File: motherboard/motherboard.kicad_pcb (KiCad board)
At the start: 4 copper layers, 177 x 88 mm, 306 parts, among them CN1 PJ-332A-6A (3.5mm Jack), IC1 PI6C557-05BLE, J1 USB_C_Receptacle, J10 DEBUG UART, J11 SYSTEM, J12 5V FAN, J13 Bus_M.2_Socket_E, J14 Micro_SD_Card_Det1, J15 Bus_M.2_Socket_M, J16 USB, J17 USB, J18 USB, J19 USB, J2 20455-040E-76 OLED IPEX, J20 CM3588 Hirose Connector, J21 5V IN, J22 BATTERY IN, J23 L829-1J1T-JM, J3 RIGHT SPEAKERS, J4 LEFT SPEAKERS, J5 Outer USB-C, J6 OLED EL POWER, J7 RTC BATTERY, J8 HDMI_A, J9 Inner USB-C, Q1 2SK3018W, Q10 2SK3018W, Q11 AO3415A, Q12 2SK3018W, Q2 2SK3018W, Q3 L2N7002WT1G, Q4 2SK3018W, Q5 2SK3018W, Q6 WNM6002-3/TR, Q7 WNM6002-3/TR, Q8 WNM6002-3/TR, Q9 WNM6002-3/TR, SW1 PWR, SW2 RESET, SW3 MASK, SW4 RECOVERY, U1 TPD4EUSB30, U10 TPD4EUSB30, U11 TPD4EUSB30, U12 TPD4EUSB30, U13 TPD4EUSB30, U14 AP2331, U16 TPD4EUSB30, U17 TPD4EUSB30, U18 TPD4EUSB30, U19 TPD4EUSB30, U2 TPD4EUSB30, U20 TPS54331DR, U21 AP2127K-3.3, U22 CH334F, U23 TPA2028D1YZFT, U24 SOT23 Hall Effect Sensor, U25 TPA2028D1YZFT, U26 AMS1117-1.8, U27 TPS54331DR, U28 SPI Flash, U3 TPD4EUSB30, U4 FUSB302BMPX, U5 SY6280AAC, U6 SY6280AAC, U7 FUSB302BMPX, U8 TPD4EUSB30, U9 TPD4EUSB30, Y1 25MHz, Y2 12MHz

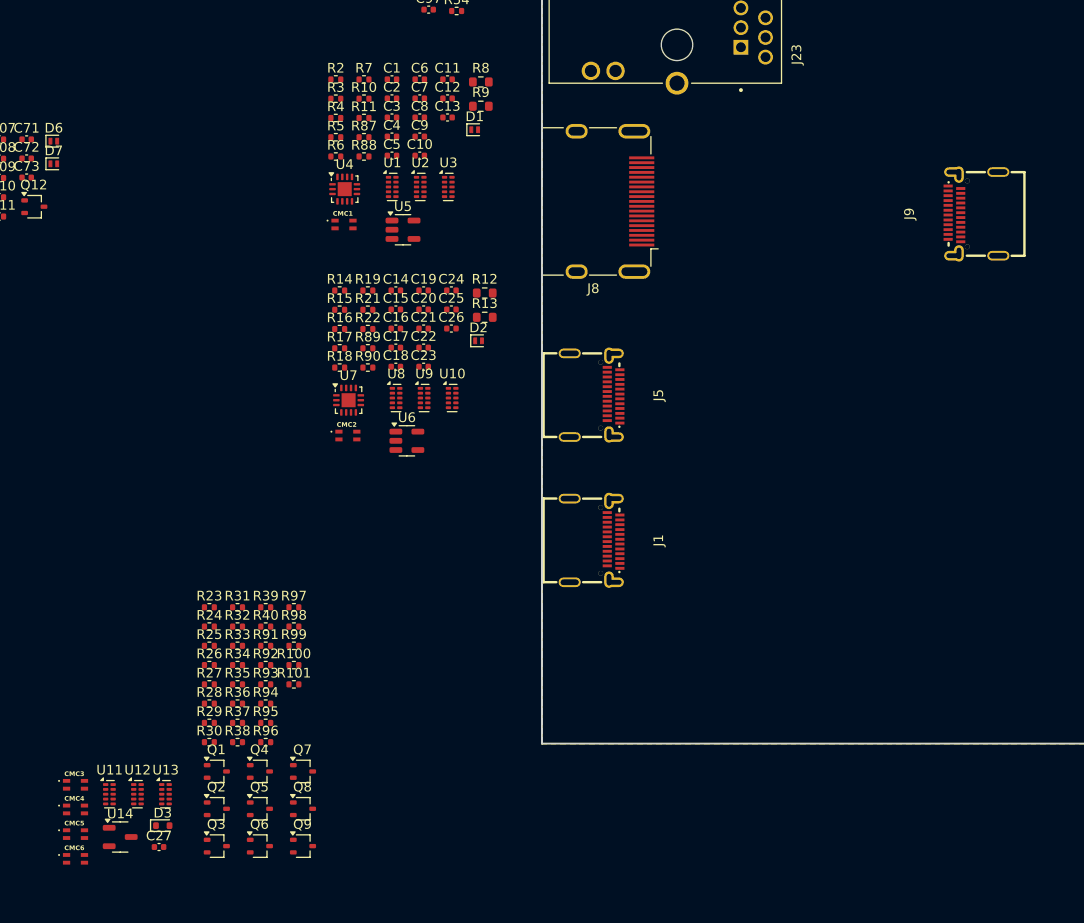
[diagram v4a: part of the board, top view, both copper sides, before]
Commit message: component placement of I/O
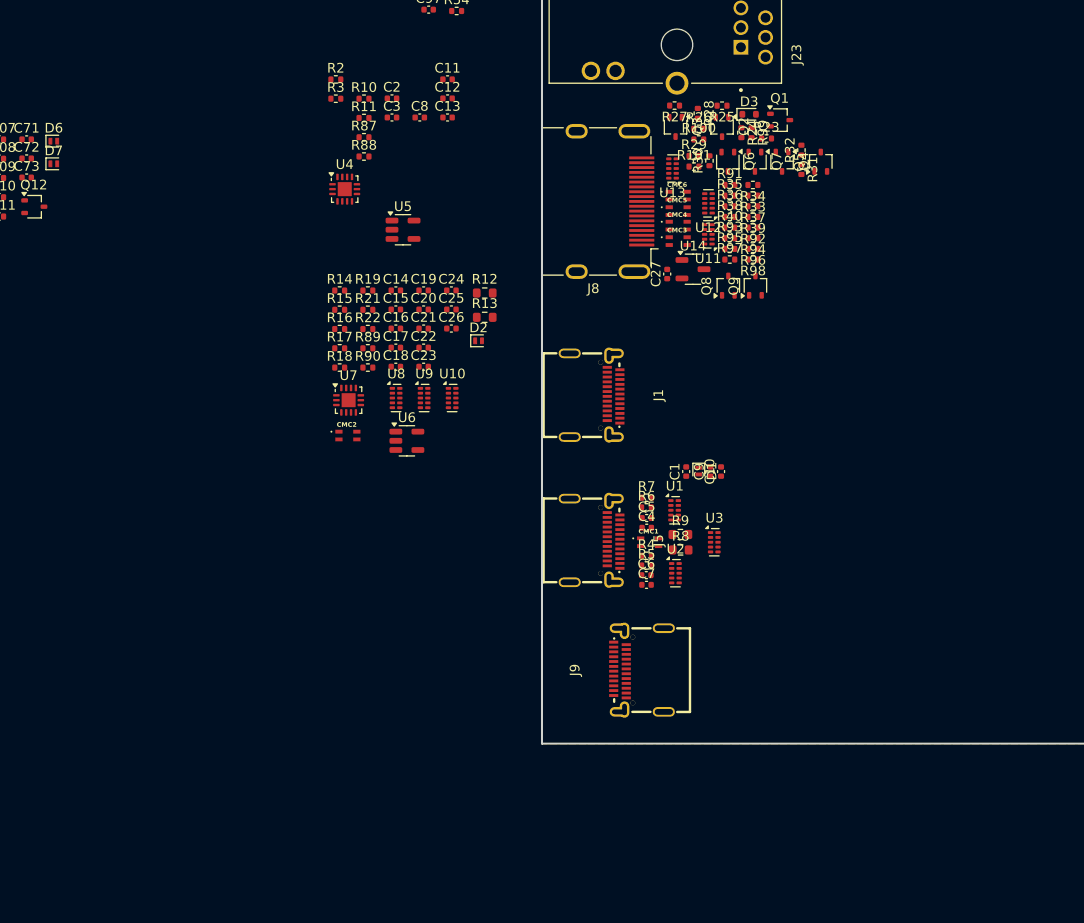
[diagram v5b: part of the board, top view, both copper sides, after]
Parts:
- moved D3 95.2 mm to (52.4, 60.0)
- moved CMC6 92.6 mm to (45.1, 68.4)
- moved CMC5 89.5 mm to (45.1, 70.0)
- moved Q1 88.9 mm to (55.6, 60.6)
- moved Q5 88.4 mm to (59.8, 64.9), turned to 90 degrees
- moved Q3 88.1 mm to (44.8, 61.3), turned to -90 degrees
- moved Q2 87.6 mm to (49.6, 61.3), turned to -90 degrees
- moved CMC4 86.7 mm to (45.1, 71.5)
- moved Q6 85.6 mm to (50.2, 64.9), turned to -90 degrees
- moved U12 84.9 mm to (48.2, 69.2), turned to 180 degrees
- moved U11 84.7 mm to (48.2, 72.4), turned to 180 degrees
- moved CMC3 83.8 mm to (45.1, 73.1)
- moved U14 83.3 mm to (46.6, 76.0)
- moved U13 83.2 mm to (44.5, 65.6), turned to 180 degrees
- moved Q4 82.9 mm to (55.8, 64.9), turned to -90 degrees
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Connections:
- CMC1 pad 1: /USBC0/IN_D- -> /USBC0/IN_D+
- CMC1 pad 2: /USBC0/IN_D+ -> /USBC0/IN_D-
- CMC1 pad 3: unconnected-(R9-Pad1) -> unconnected-(R8-Pad1)
- CMC1 pad 4: unconnected-(R8-Pad1) -> unconnected-(R9-Pad1)
- CMC10 pad 1: /P25G_MDIP3 -> /P25G_MDIN3
- CMC10 pad 2: /P25G_MDIN3 -> /P25G_MDIP3
- CMC10 pad 3: /Ethernet/N3 -> /Ethernet/P3
- CMC10 pad 4: /Ethernet/P3 -> /Ethernet/N3
- CMC3 pad 3: /HDMI_TX/HDMI0_TX2N_PORT -> /HDMI_TX/HDMI0_TX2P_PORT
- CMC3 pad 4: /HDMI_TX/HDMI0_TX2P_PORT -> /HDMI_TX/HDMI0_TX2N_PORT
- CMC4 pad 3: /HDMI_TX/HDMI0_TX1N_PORT -> /HDMI_TX/HDMI0_TX1P_PORT
- CMC4 pad 4: /HDMI_TX/HDMI0_TX1P_PORT -> /HDMI_TX/HDMI0_TX1N_PORT
- CMC5 pad 3: /HDMI_TX/HDMI0_TX0N_PORT -> /HDMI_TX/HDMI0_TX0P_PORT
- CMC5 pad 4: /HDMI_TX/HDMI0_TX0P_PORT -> /HDMI_TX/HDMI0_TX0N_PORT
- CMC6 pad 3: /HDMI_TX/HDMI0_TX3N_PORT -> /HDMI_TX/HDMI0_TX3P_PORT
- CMC6 pad 4: /HDMI_TX/HDMI0_TX3P_PORT -> /HDMI_TX/HDMI0_TX3N_PORT
- CMC7 pad 1: /P25G_MDIP2 -> /P25G_MDIN2
- CMC7 pad 2: /P25G_MDIN2 -> /P25G_MDIP2
- CMC7 pad 3: /Ethernet/N0 -> /Ethernet/P0
- CMC7 pad 4: /Ethernet/P0 -> /Ethernet/N0
- CMC8 pad 1: /P25G_MDIP1 -> /P25G_MDIN1
- CMC8 pad 2: /P25G_MDIN1 -> /P25G_MDIP1
- CMC8 pad 3: /Ethernet/N1 -> /Ethernet/P1
- CMC8 pad 4: /Ethernet/P1 -> /Ethernet/N1
- CMC9 pad 1: /P25G_MDIP0 -> /P25G_MDIN0
- CMC9 pad 2: /P25G_MDIN0 -> /P25G_MDIP0
- CMC9 pad 3: /Ethernet/N2 -> /Ethernet/P2
- CMC9 pad 4: /Ethernet/P2 -> /Ethernet/N2
- J1 pad A6: Net-(CMC2-Pad2) -> Net-(CMC2-Pad1)
- J1 pad A7: Net-(CMC2-Pad1) -> Net-(CMC2-Pad2)
- J1 pad B6: Net-(CMC2-Pad2) -> Net-(CMC2-Pad1)
- J1 pad B7: Net-(CMC2-Pad1) -> Net-(CMC2-Pad2)
- J8 pad 1: unconnected-(CMC3-Pad1) -> unconnected-(CMC3-Pad2)
- J8 pad 10: unconnected-(CMC6-Pad1) -> unconnected-(CMC6-Pad2)
- J8 pad 12: unconnected-(CMC6-Pad2) -> unconnected-(CMC6-Pad1)
- J8 pad 3: unconnected-(CMC3-Pad2) -> unconnected-(CMC3-Pad1)
- J8 pad 4: unconnected-(CMC4-Pad1) -> unconnected-(CMC4-Pad2)
- J8 pad 6: unconnected-(CMC4-Pad2) -> unconnected-(CMC4-Pad1)
- J8 pad 7: unconnected-(CMC5-Pad1) -> unconnected-(CMC5-Pad2)
- J8 pad 9: unconnected-(CMC5-Pad2) -> unconnected-(CMC5-Pad1)
- R12 pad 1: Net-(CMC2-Pad4) -> Net-(CMC2-Pad3)
- R13 pad 1: Net-(CMC2-Pad3) -> Net-(CMC2-Pad4)
- U1 pad 10: unconnected-(U1-NC-Pad10) -> /USBC0/RX1+
- U1 pad 6: unconnected-(U1-NC-Pad6) -> /USBC0/TX1-
- U1 pad 7: unconnected-(U1-NC-Pad7) -> /USBC0/TX1+
- U1 pad 9: unconnected-(U1-NC-Pad9) -> /USBC0/RX1-
- U11 pad 10: unconnected-(U11-NC-Pad10) -> /HDMI_TX/HDMI0_TX2P_PORT
- U11 pad 6: unconnected-(U11-NC-Pad6) -> /HDMI_TX/HDMI0_TX1N_PORT
- U11 pad 7: unconnected-(U11-NC-Pad7) -> /HDMI_TX/HDMI0_TX1P_PORT
- U11 pad 9: unconnected-(U11-NC-Pad9) -> /HDMI_TX/HDMI0_TX2N_PORT
- U12 pad 10: unconnected-(U12-NC-Pad10) -> /HDMI_TX/HDMI0_TX0P_PORT
- U12 pad 6: unconnected-(U12-NC-Pad6) -> /HDMI_TX/HDMI0_TX3N_PORT
- U12 pad 7: unconnected-(U12-NC-Pad7) -> /HDMI_TX/HDMI0_TX3P_PORT
- U12 pad 9: unconnected-(U12-NC-Pad9) -> /HDMI_TX/HDMI0_TX0N_PORT
- U13 pad 10: unconnected-(U13-NC-Pad10) -> /HDMI_TX/CEC
- U13 pad 2: /HDMI_TX/HDMI0_5V -> /HDMI_TX/SBDP
- U13 pad 4: /HDMI_TX/SBDP -> /HDMI_TX/HDMI0_5V
- U13 pad 6: unconnected-(U13-NC-Pad6) -> /HDMI_TX/SBDN
- U13 pad 7: unconnected-(U13-NC-Pad7) -> /HDMI_TX/HDMI0_5V
- U13 pad 9: unconnected-(U13-NC-Pad9) -> /HDMI_TX/SBDP
- U2 pad 10: unconnected-(U2-NC-Pad10) -> /USBC0/RX2-
- U2 pad 4: /USBC0/TX2+ -> /USBC0/TX2-
- U2 pad 5: /USBC0/TX2- -> /USBC0/TX2+
- U2 pad 6: unconnected-(U2-NC-Pad6) -> /USBC0/TX2+
- U2 pad 7: unconnected-(U2-NC-Pad7) -> /USBC0/TX2-
- U2 pad 9: unconnected-(U2-NC-Pad9) -> /USBC0/RX2+
- U3 pad 10: unconnected-(U3-NC-Pad10) -> /USBC0/D+
- U3 pad 4: /USBC0/SBUS1 -> /USBC0/SBUS2
- U3 pad 5: /USBC0/SBUS2 -> /USBC0/SBUS1
- U3 pad 6: unconnected-(U3-NC-Pad6) -> /USBC0/SBUS1
- U3 pad 7: unconnected-(U3-NC-Pad7) -> /USBC0/SBUS2
- U3 pad 9: unconnected-(U3-NC-Pad9) -> /USBC0/D-

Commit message: placement roughly halfway done
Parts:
- removed C17, C18, C21, C22, C33, C34, C4, C5, C6, C7: 100nF, Capacitor_SMD:C_0402_1005Metric
- removed C37, C38, C39, C40, C41, C42, C43, C44: 220nF, Capacitor_SMD:C_0402_1005Metric
- removed D1, D2: LESD8D5.0CB1T5G, Diode_SMD:D_SOD-882
- removed R12, R13, R8, R9: 2.2R, Resistor_SMD:R_0603_1608Metric
- removed R14, R15, R16, R17, R4, R5, R6, R7: 0R, Resistor_SMD:R_0402_1005Metric
- added U15: TVS2200DRV, Package_SON:WSON-6-1EP_2x2mm_P0.65mm_EP1x1.6mm, F.Cu at (34.1, 39.6)
- added U29: TVS2200DRV, Package_SON:WSON-6-1EP_2x2mm_P0.65mm_EP1x1.6mm, F.Cu at (76.5, 64.6)
- C1, C14: value 100nF -> 100nF (+25V)
- C10, C15, C16, C9: value 10uF -> 10uF (C913517); footprint Capacitor_SMD:C_0402_1005Metric -> Capacitor_SMD:C_0603_1608Metric
- C94, C95, C96, C97: footprint Capacitor_SMD:C_0402_1005Metric -> Capacitor_SMD:C_0805_2012Metric
- U1, U10, U11, U12, U13, U16, U17, U18, U19, U2, U3, U8, U9: value TPD4EUSB30 -> TPD4E02B04
- moved CN1 203.3 mm to (141.5, 156.5), turned to 180 degrees
- moved R102 195.2 mm to (145.7, 151.7), turned to 180 degrees
- moved R104 190.5 mm to (137.0, 161.8), turned to 180 degrees
- moved R107 186.8 mm to (134.5, 159.7)
- moved D7 186.8 mm to (140.8, 161.1), turned to -90 degrees
- moved R103 186.6 mm to (137.3, 151.2), turned to 180 degrees
- moved R106 185.4 mm to (133.6, 161.4), turned to -90 degrees
- moved C72 184.7 mm to (135.1, 161.4), turned to 90 degrees
- moved R109 184.3 mm to (135.2, 157.6), turned to -90 degrees
- moved R108 182.7 mm to (134.7, 153.2)
- moved R110 182.4 mm to (135.2, 155.6), turned to -90 degrees
- moved D6 182.0 mm to (139.5, 151.5), turned to 90 degrees
- moved R105 181.9 mm to (133.8, 151.6), turned to 90 degrees
- moved R111 181.4 mm to (133.7, 158.2)
- moved C71 180.9 mm to (135.3, 151.6), turned to -90 degrees
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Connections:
- net Net-(U25-EN) renamed /Audio/SPK_EN_L
- CMC1 pad 3: unconnected-(R8-Pad1) -> /USBC0/D-
- CMC1 pad 4: unconnected-(R9-Pad1) -> /USBC0/D+
- CMC2 pad 3: Net-(CMC2-Pad3) -> /USBC1/D-
- CMC2 pad 4: Net-(CMC2-Pad4) -> /USBC1/D+
- J1 pad A10: Net-(J1-RX2-) -> /USBC1/RX2-
- J1 pad A11: Net-(J1-RX2+) -> /USBC1/RX2+
- J1 pad A2: Net-(J1-TX1+) -> /USBC1/TX1+
- J1 pad A3: Net-(J1-TX1-) -> /USBC1/TX1-
- J1 pad B10: Net-(J1-RX1-) -> /USBC1/RX1-
- J1 pad B11: Net-(J1-RX1+) -> /USBC1/RX1+
- J1 pad B2: Net-(J1-TX2+) -> /USBC1/TX2+
- J1 pad B3: Net-(J1-TX2-) -> /USBC1/TX2-
- J13 pad 35: unconnected-(C33-Pad2) -> /PCIE20_1_TXP
- J13 pad 37: unconnected-(C34-Pad2) -> /PCIE20_1_TXN
- J15 pad 11: Net-(J15-PETn3) -> /PCIE30_PORT1_TX3N
- J15 pad 13: Net-(J15-PETp3) -> /PCIE30_PORT1_TX3P
- J15 pad 23: Net-(J15-PETn2) -> /PCIE30_PORT1_TX2N
- J15 pad 25: Net-(J15-PETp2) -> /PCIE30_PORT1_TX2P
- J15 pad 35: Net-(J15-PETn1) -> /PCIE30_PORT0_TX1N
- J15 pad 37: Net-(J15-PETp1) -> /PCIE30_PORT0_TX1P
- J15 pad 47: Net-(J15-PETn0/SATA-A-) -> /PCIE30_PORT0_TX0N
- J15 pad 49: Net-(J15-PETp0/SATA-A+) -> /PCIE30_PORT0_TX0P
- J5 pad A10: /USBC0/IN_RX2- -> /USBC0/RX2-
- J5 pad A11: /USBC0/IN_RX2+ -> /USBC0/RX2+
- J5 pad A2: /USBC0/IN_TX1+ -> /USBC0/TX1+
- J5 pad A3: /USBC0/IN_TX1- -> /USBC0/TX1-
- J5 pad B10: /USBC0/IN_RX1- -> /USBC0/RX1-
- J5 pad B11: /USBC0/IN_RX1+ -> /USBC0/RX1+
- J5 pad B2: /USBC0/IN_TX2+ -> /USBC0/TX2+
- J5 pad B3: /USBC0/IN_TX2- -> /USBC0/TX2-
- J9 pad A10: /USBC0/IN_RX2- -> /USBC0/RX2-
- J9 pad A11: /USBC0/IN_RX2+ -> /USBC0/RX2+
- J9 pad A2: /USBC0/IN_TX1+ -> /USBC0/TX1+
- J9 pad A3: /USBC0/IN_TX1- -> /USBC0/TX1-
- J9 pad B10: /USBC0/IN_RX1- -> /USBC0/RX1-
- J9 pad B11: /USBC0/IN_RX1+ -> /USBC0/RX1+
- J9 pad B2: /USBC0/IN_TX2+ -> /USBC0/TX2+
- J9 pad B3: /USBC0/IN_TX2- -> /USBC0/TX2-
- R118 pad 2: /Audio/SPK_EN -> /Audio/SPK_EN_R
- U16 pad 10: unconnected-(U16-NC-Pad10) -> /Ethernet/P2
- U16 pad 6: unconnected-(U16-NC-Pad6) -> /Ethernet/N3
- U16 pad 7: unconnected-(U16-NC-Pad7) -> /Ethernet/P3
- U16 pad 9: unconnected-(U16-NC-Pad9) -> /Ethernet/N2
- U17 pad 10: unconnected-(U17-NC-Pad10) -> /Ethernet/P0
- U17 pad 6: unconnected-(U17-NC-Pad6) -> /Ethernet/N1
- U17 pad 7: unconnected-(U17-NC-Pad7) -> /Ethernet/P1
- U17 pad 9: unconnected-(U17-NC-Pad9) -> /Ethernet/N0
- U23 pad B1: Net-(J3-Pin_1) -> Net-(J3-Pin_2)
- U23 pad B2: /Audio/SPK_EN -> /Audio/SPK_EN_R
- U23 pad C1: Net-(J3-Pin_2) -> Net-(J3-Pin_1)
- U25 pad B1: Net-(J4-Pin_1) -> Net-(J4-Pin_2)
- U25 pad C1: Net-(J4-Pin_2) -> Net-(J4-Pin_1)
- U3 pad 1: /USBC0/D+ -> /USBC0/SBUS2
- U3 pad 10: /USBC0/D+ -> /USBC0/SBUS2
- U3 pad 2: /USBC0/D- -> /USBC0/D+
- U3 pad 4: /USBC0/SBUS2 -> /USBC0/D-
- U3 pad 7: /USBC0/SBUS2 -> /USBC0/D-
- U3 pad 9: /USBC0/D- -> /USBC0/D+

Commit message: layout nearing completion
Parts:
- removed J7: RTC BATTERY, Connector_PinHeader_2.54mm:PinHeader_1x02_P2.54mm_Horizontal
- added C17: 10uF, Capacitor_SMD:C_0603_1608Metric, F.Cu at (64.8, 38.5)
- added C18: 0.1uF, Capacitor_SMD:C_0402_1005Metric, F.Cu at (62.7, 38.3)
- added C21: 10uF, Capacitor_SMD:C_0603_1608Metric, F.Cu at (73.3, 38.5)
- added C22: 0.1uF, Capacitor_SMD:C_0402_1005Metric, F.Cu at (71.2, 38.3)
- added C4: 10uF, Capacitor_SMD:C_0603_1608Metric, F.Cu at (64.7, 51.9)
- added C5: 0.1uF, Capacitor_SMD:C_0402_1005Metric, F.Cu at (62.6, 51.8)
- added C6: 10uF, Capacitor_SMD:C_0603_1608Metric, F.Cu at (73.3, 52.0)
- added C7: 0.1uF, Capacitor_SMD:C_0402_1005Metric, F.Cu at (71.2, 51.8)
- C11, C12, C13, C19, C20, C24, C32, C50, C52, C67, C69, C74, C77, C80, C81, C83, C87, C88, C92, C93: footprint Capacitor_SMD:C_0402_1005Metric -> Capacitor_SMD:C_0603_1608Metric
- J3, J4: footprint Connector_PinHeader_2.54mm:PinHeader_1x02_P2.54mm_Horizontal -> Connector_PinHeader_2.54mm:PinHeader_1x02_P2.54mm_Vertical
- R86: footprint Resistor_SMD:R_0402_1005Metric -> Jumper:SolderJumper-2_P1.3mm_Open_TrianglePad1.0x1.5mm
- moved D5 248.4 mm to (183.6, 93.4), turned to 90 degrees
- moved C52 245.3 mm to (179.3, 86.5)
- moved C50 245.1 mm to (184.3, 99.8), turned to 90 degrees
- moved C51 244.7 mm to (184.1, 102.5), turned to -90 degrees
- moved C49 242.6 mm to (181.0, 95.0), turned to -90 degrees
- moved C62 239.5 mm to (187.0, 106.6), turned to -90 degrees
- moved C63 239.5 mm to (186.9, 108.5), turned to 90 degrees
- moved C58 238.9 mm to (182.2, 107.3), turned to 90 degrees
- moved C69 238.0 mm to (179.3, 88.2)
- moved C60 235.9 mm to (184.9, 110.8), turned to 90 degrees
- moved C61 235.1 mm to (183.8, 110.8), turned to 90 degrees
- moved C55 235.0 mm to (177.4, 98.4), turned to -90 degrees
- moved C53 234.9 mm to (175.6, 88.3), turned to 90 degrees
- moved C59 234.2 mm to (176.8, 107.2), turned to 90 degrees
- moved C57 233.9 mm to (180.3, 120.3)
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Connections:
- C28 pad 1: /System/PWRON_L -> /PWRON_L
- C29 pad 1: /System/RESET_L -> /RESET_L
- C31 pad 1: /System/RECOVERY -> /RECOVERY
- J11 pad 5: /System/RESET_L -> /System/RESET_L_IN
- J11 pad 6: /System/PWRON_L -> /System/PWRON_L_IN
- J20 pad 101: /System/RECOVERY -> /RECOVERY
- J20 pad 16: /System/RESET_L -> /RESET_L
- J20 pad 17: /System/PWRON_L -> /PWRON_L
- R41 pad 1: /System/PWRON_L -> /PWRON_L
- R41 pad 2: /System/PWRON_L -> /System/PWRON_L_IN
- R42 pad 1: /System/RESET_L -> /RESET_L
- R42 pad 2: /System/RESET_L -> /System/RESET_L_IN
- R44 pad 1: /System/RECOVERY -> /RECOVERY
- R44 pad 2: /System/RECOVERY -> /System/RECOVERY_IN
- SW1 pad 1: /System/PWRON_L -> /System/PWRON_L_IN
- SW2 pad 1: /System/RESET_L -> /System/RESET_L_IN
- SW4 pad 1: /System/RECOVERY -> /System/RECOVERY_IN
- U10 pad 10: unconnected-(U10-NC-Pad10) -> /USBC1/RX2-
- U10 pad 4: /USBC1/TX2+ -> /USBC1/TX2-
- U10 pad 5: /USBC1/TX2- -> /USBC1/TX2+
- U10 pad 6: unconnected-(U10-NC-Pad6) -> /USBC1/TX2+
- U10 pad 7: unconnected-(U10-NC-Pad7) -> /USBC1/TX2-
- U10 pad 9: unconnected-(U10-NC-Pad9) -> /USBC1/RX2+
- U8 pad 1: /USBC1/D+ -> /USBC1/SBUS2
- U8 pad 10: unconnected-(U8-NC-Pad10) -> /USBC1/SBUS2
- U8 pad 2: /USBC1/D- -> /USBC1/D+
- U8 pad 4: /USBC1/SBUS1 -> /USBC1/D-
- U8 pad 5: /USBC1/SBUS2 -> /USBC1/SBUS1
- U8 pad 6: unconnected-(U8-NC-Pad6) -> /USBC1/SBUS1
- U8 pad 7: unconnected-(U8-NC-Pad7) -> /USBC1/D-
- U8 pad 9: unconnected-(U8-NC-Pad9) -> /USBC1/D+
- U9 pad 10: unconnected-(U9-NC-Pad10) -> /USBC1/RX1+
- U9 pad 6: unconnected-(U9-NC-Pad6) -> /USBC1/TX1-
- U9 pad 7: unconnected-(U9-NC-Pad7) -> /USBC1/TX1+
- U9 pad 9: unconnected-(U9-NC-Pad9) -> /USBC1/RX1-
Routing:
- net /SD Card/D2: track 5.83 -> 0.00 mm
- net /SD Card/CMD: track 5.44 -> 0.00 mm
- net /SD Card/DET: track 5.32 -> 0.00 mm
- net /SD Card/D0: track 5.03 -> 0.00 mm
- net /SD Card/D1: track 4.98 -> 0.00 mm
- net /SD Card/D3: track 4.56 -> 0.00 mm
- net /SD Card/CLK: track 4.18 -> 0.00 mm
- net /SD Card/VDD: track 2.62 -> 0.00 mm
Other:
- board size 177 x 88 mm -> 177 x 92 mm
